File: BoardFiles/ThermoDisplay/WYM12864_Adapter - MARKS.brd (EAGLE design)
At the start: 110 x 64.1 mm, 6 parts, among them J1 JMP_3WAY, U1 PCA8575DSOIC-24

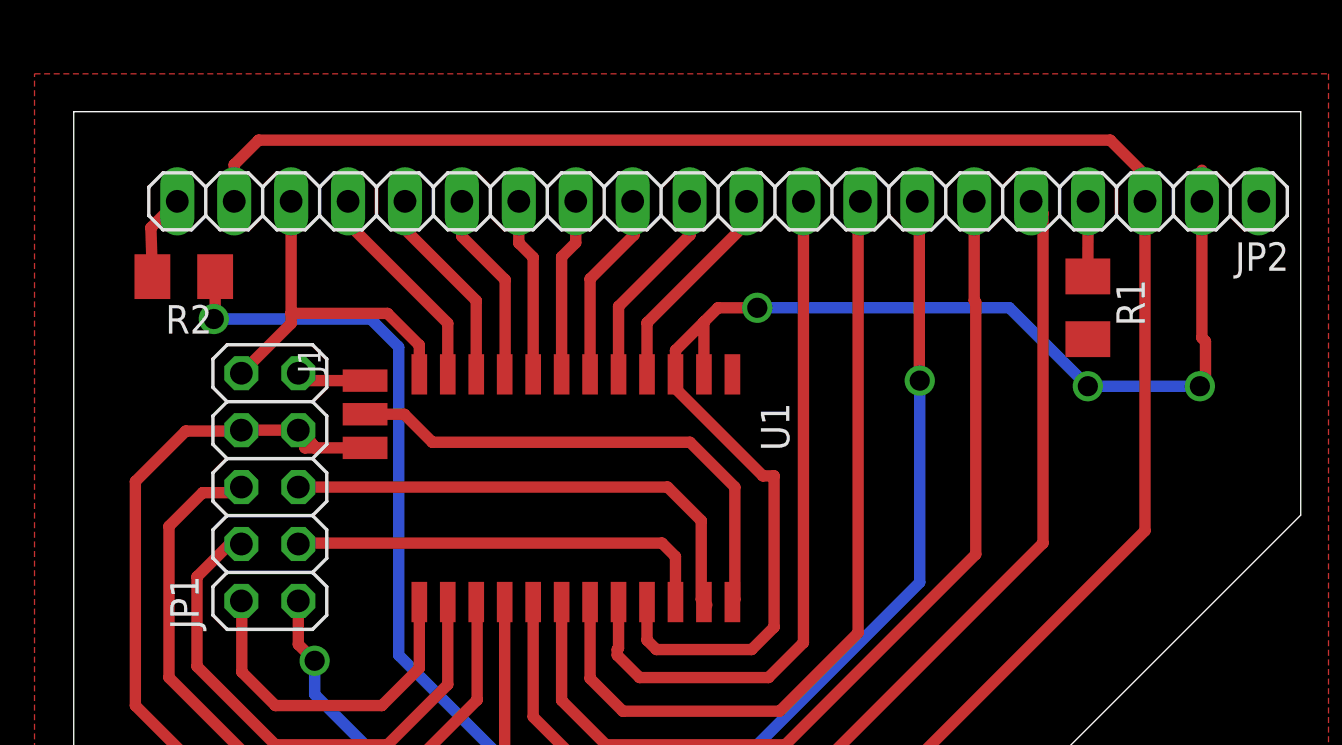
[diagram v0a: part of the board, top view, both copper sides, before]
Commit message: Fixed board schematic/board errors
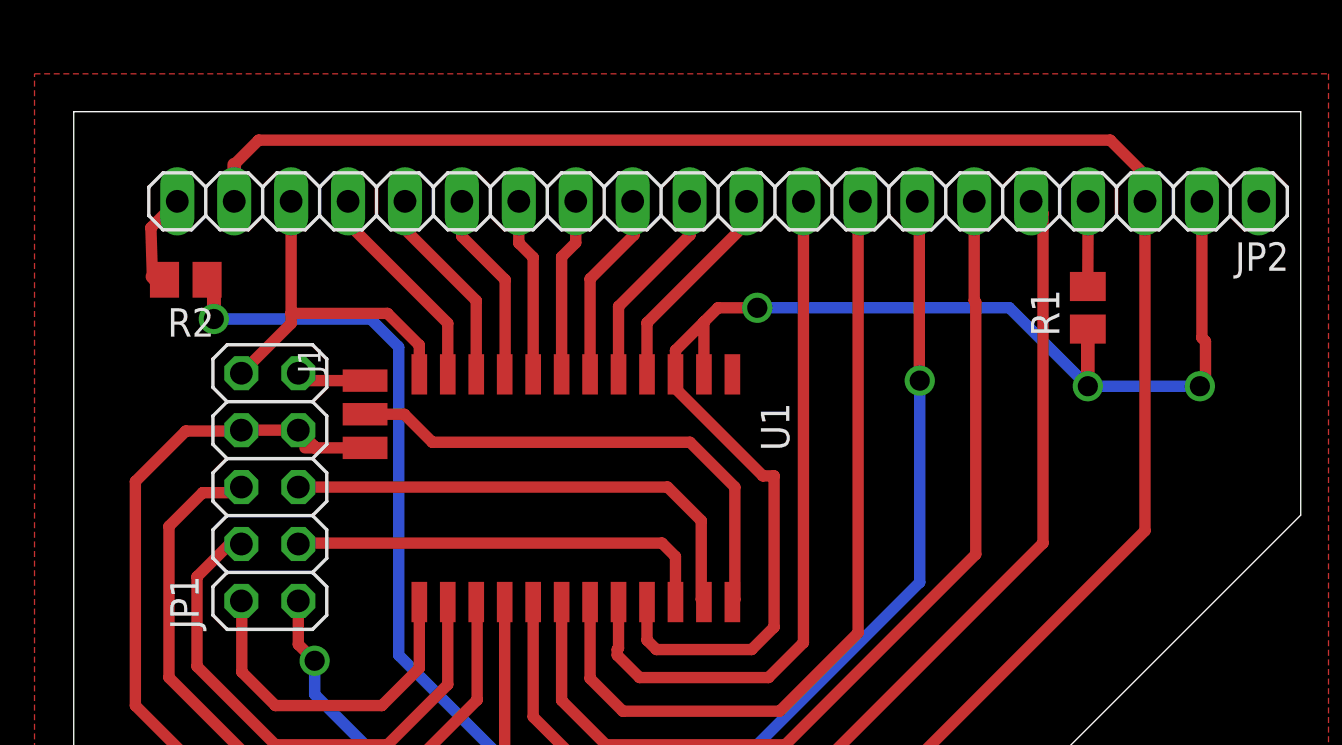
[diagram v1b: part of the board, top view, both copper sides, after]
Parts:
- R1, R2: device rcl:M1206 -> DR:M0805
- moved R2 0.17 mm to (5.00, 26.8)
- turned R1 to 90 degrees
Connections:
- net GND: now also R1.1; no longer R1.2
- net N$2: now also R1.2; no longer R1.1
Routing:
- net +5V: track 137.2 -> 133.5 mm
- net BL_K: track 38.3 -> 40.2 mm
- net N$7: track 3.85 -> 4.45 mm
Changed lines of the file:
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@@
 </autorouter>
 <elements>
-<element name="R2" library="rcl" library_urn="urn:adsk.eagle:library:334" package="M1206" package3d_urn="urn:adsk.eagle:package:23566/2" value="" x="4.91" y="26.89" smashed="yes" rot="R180">
-<attribute name="NAME" x="6.18" y="25.62" size="1.27" layer="25" rot="R180"/>
-<attribute name="POPULARITY" value="22" x="4.91" y="26.89" size="1.778" layer="27" rot="R180" display="off"/>
-<attribute name="SPICEPREFIX" value="R" x="4.91" y="26.89" size="1.778" layer="27" rot="R180" display="off"/>
-<attribute name="VALUE" x="6.18" y="29.43" size="1.27" layer="27" rot="R180"/>
-</element>
 <element name="U1" library="DR" package="SOIC-24" value="PCA8575DSOIC-24" x="29.39" y="22.53" smashed="yes" rot="R270">
 <attribute name="NAME" x="30.66" y="21.26" size="1.27" layer="25" rot="R270"/>
@@
 <attribute name="VALUE" x="13.195" y="11.15" size="1.27" layer="27" rot="R90"/>
 </element>
-<element name="R1" library="rcl" library_urn="urn:adsk.eagle:library:334" package="M1206" package3d_urn="urn:adsk.eagle:package:23566/2" value="" x="45.25" y="25.5" smashed="yes" rot="R270">
-<attribute name="NAME" x="46.52" y="26.77" size="1.27" layer="25" rot="R270"/>
-<attribute name="POPULARITY" value="22" x="45.25" y="25.5" size="1.778" layer="27" rot="R270" display="off"/>
-<attribute name="SPICEPREFIX" value="R" x="45.25" y="25.5" size="1.778" layer="27" rot="R270" display="off"/>
-<attribute name="VALUE" x="42.71" y="26.77" size="1.27" layer="27" rot="R270"/>
-</element>
 <element name="J1" library="DR" package="JUMPER_THREEWAY" value="JMP_3WAY" x="13" y="20.75" smashed="yes" rot="R270">
 <attribute name="NAME" x="10" y="23.75" size="1.016" layer="25" rot="R270"/>
+</element>
+<element name="R1" library="DR" package="M0805" value="" x="45.25" y="25.5" smashed="yes" rot="R90">
+<attribute name="NAME" x="43.98" y="24.23" size="1.27" layer="25" rot="R90"/>
+<attribute name="VALUE" x="47.79" y="24.23" size="1.27" layer="27" rot="R90"/>
+</element>
+<element name="R2" library="DR" package="M0805" value="" x="5" y="26.75" smashed="yes" rot="R180">
+<attribute name="NAME" x="6.27" y="25.48" size="1.27" layer="25" rot="R180"/>
+<attribute name="VALUE" x="6.27" y="29.29" size="1.27" layer="27" rot="R180"/>
 </element>
 </elements>
@@
 <contactref element="U1" pad="2"/>
 <contactref element="JP2" pad="2"/>
-<contactref element="R1" pad="2"/>
 <contactref element="JP2" pad="18"/>
-<wire x1="9.7" y1="30.25" x2="9.75" y2="30.3" width="0.508" layer="1"/>
-<wire x1="50.34" y1="31.64" x2="50.34" y2="30.25" width="0.508" layer="1"/>
 <contactref element="JP1" pad="10"/>
 <wire x1="28.12" y1="22.53" x2="28.12" y2="24.87" width="0.508" layer="1"/>
@@
 <wire x1="41.75" y1="25.5" x2="45.25" y2="22" width="0.508" layer="16"/>
 <via x="45.25" y="22" extent="1-16" drill="0.9" diameter="1.2"/>
-<wire x1="45.25" y1="22" x2="45" y2="21.75" width="0.508" layer="1"/>
 <wire x1="45" y1="21.75" x2="45.125" y2="21.625" width="0.508" layer="1"/>
-<wire x1="45.125" y1="21.625" x2="45.25" y2="21.75" width="0.508" layer="1"/>
 <wire x1="50.34" y1="30.25" x2="50.34" y2="24.16" width="0.508" layer="1"/>
 <wire x1="50.34" y1="24.16" x2="50.5" y2="24" width="0.508" layer="1"/>
@@
 <wire x1="25.58" y1="10.67" x2="26" y2="10.25" width="0.508" layer="1"/>
 <wire x1="26" y1="10.25" x2="30.25" y2="10.25" width="0.508" layer="1"/>
+<wire x1="45.25" y1="24.1" x2="45.25" y2="22" width="0.6096" layer="1"/>
+<wire x1="45.25" y1="22" x2="45" y2="21.75" width="0.6096" layer="1"/>
+<contactref element="R1" pad="1"/>
 </signal>
 <signal name="N$2">
 <contactref element="JP2" pad="4"/>
-<contactref element="R1" pad="1"/>
 <wire x1="45.25" y1="26.9" x2="45.264203125" y2="30.245796875" width="0.508" layer="1"/>
 <wire x1="45.26" y1="30.25" x2="45.264203125" y2="30.245796875" width="0.508" layer="1"/>
+<contactref element="R1" pad="2"/>
+<wire x1="45.25" y1="26.45" x2="45.25" y2="26.9" width="0" layer="19" extent="1-1"/>
 </signal>
 <signal name="D2">
@@
 <signal name="SDA">
 <contactref element="U1" pad="23"/>
-<wire x1="28.25" y1="12.24" x2="28.12" y2="12.37" width="0.508" layer="1"/>
 <contactref element="JP1" pad="5"/>
 <wire x1="28.12" y1="12.37" x2="28" y2="12.49" width="0.508" layer="1"/>
@@
 </signal>
 <signal name="N$7">
-<contactref element="R2" pad="2"/>
 <contactref element="JP2" pad="20"/>
 <wire x1="3.51" y1="26.89" x2="3.4425" y2="29.0725" width="0.508" layer="1"/>
 <wire x1="3.4425" y1="29.0725" x2="4.62" y2="30.25" width="0.508" layer="1"/>
+<contactref element="R2" pad="2"/>
+<wire x1="4.05" y1="26.75" x2="3.65" y2="26.75" width="0.6096" layer="1"/>
+<wire x1="3.65" y1="26.75" x2="3.51" y2="26.89" width="0.6096" layer="1"/>
 </signal>
 <signal name="RD">
@@
 <contactref element="JP2" pad="19"/>
 <contactref element="J1" pad="2"/>
-<wire x1="7.16" y1="30.25" x2="7.16" y2="31.57" width="0.508" layer="1"/>
-<wire x1="47.75" y1="29.5" x2="47.75" y2="30.2" width="0.508" layer="1"/>
 <wire x1="47.75" y1="30.2" x2="47.8" y2="30.25" width="0.508" layer="1"/>
-<wire x1="10.6" y1="19.5" x2="10.31698125" y2="19.25" width="0.508" layer="1"/>
 <wire x1="13" y1="19.25" x2="10.75" y2="19.25" width="0.508" layer="1"/>
 <wire x1="10.75" y1="19.25" x2="10.31698125" y2="19.25" width="0.508" layer="1"/>
-<wire x1="7.16" y1="30.25" x2="7.25" y2="30.16" width="0.508" layer="1"/>
-<wire x1="7.25" y1="30.16" x2="7.25" y2="29" width="0.508" layer="1"/>
 <contactref element="JP1" pad="7"/>
 <contactref element="JP1" pad="8"/>
@@
 <wire x1="47.8" y1="15.55" x2="47.8" y2="30.25" width="0.508" layer="1"/>
 <wire x1="35.25" y1="3" x2="47.8" y2="15.55" width="0.508" layer="1"/>
-<wire x1="7.16" y1="30.25" x2="7.16" y2="31.89" width="0.508" layer="1"/>
-<wire x1="7.16" y1="31.89" x2="8.25" y2="32.98" width="0.508" layer="1"/>
+<wire x1="8.25" y1="32.98" x2="7.16" y2="31.89" width="0.508" layer="1"/>
 <wire x1="8.25" y1="32.98" x2="46.25" y2="32.98" width="0.508" layer="1"/>
 <wire x1="46.25" y1="32.98" x2="47.75" y2="31.48" width="0.508" layer="1"/>
 <wire x1="47.75" y1="30.3" x2="47.8" y2="30.25" width="0.508" layer="1"/>
 <wire x1="47.75" y1="31.48" x2="47.75" y2="30.3" width="0.508" layer="1"/>
+<wire x1="7.16" y1="31.89" x2="7.16" y2="30.25" width="0.6096" layer="1"/>
 </signal>
 <signal name="CMD">
@@
 <contactref element="JP2" pad="17"/>
 <contactref element="U1" pad="11"/>
-<wire x1="16.75" y1="22.59" x2="16.69" y2="22.53" width="0.508" layer="1"/>
 <wire x1="16.69" y1="22.53" x2="16.69" y2="24.81" width="0.508" layer="1"/>
 <wire x1="12.24" y1="29.26" x2="12.24" y2="30.25" width="0.508" layer="1"/>
@@
 </signal>
 <signal name="BL_K">
-<contactref element="R2" pad="1"/>
 <contactref element="U1" pad="16"/>
 <wire x1="19.23" y1="12.37" x2="19.23" y2="5.52" width="0.508" layer="1"/>
@@
 <wire x1="6.25" y1="25" x2="6.31" y2="25" width="0.508" layer="1"/>
 <wire x1="6.31" y1="26.89" x2="6.31" y2="25" width="0.508" layer="1"/>
+<contactref element="R2" pad="1"/>
+<wire x1="5.95" y1="26.75" x2="6.25" y2="26.45" width="0.6096" layer="1"/>
+<wire x1="6.25" y1="26.45" x2="6.25" y2="25" width="0.6096" layer="1"/>
 </signal>
 <signal name="N$3">
